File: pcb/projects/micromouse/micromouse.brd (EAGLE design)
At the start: 80 x 100 mm, 52 parts, among them M1 332-06, M2 332-06, U1 DSPIC33FJ64MC804-H/PTTQFP44_1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, U2 UA78M33CKCS, U3 UA78M05CKCS

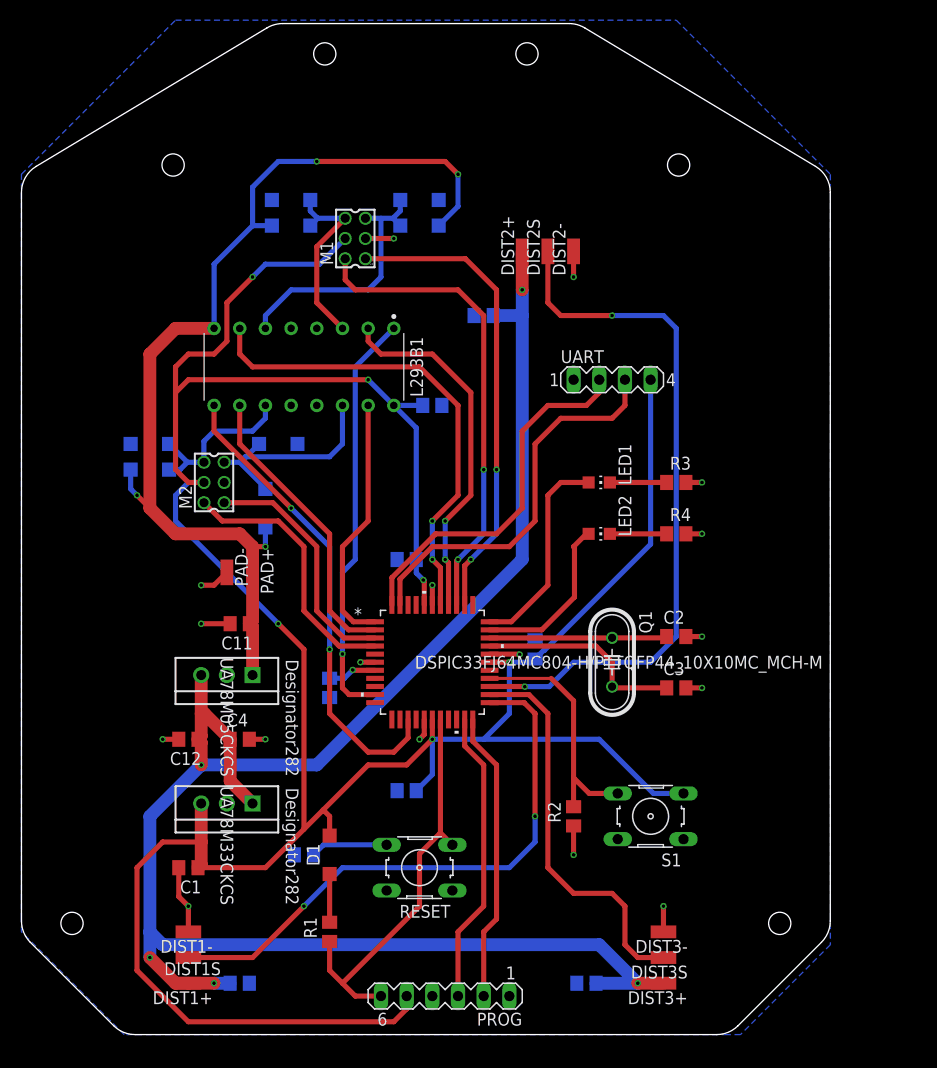
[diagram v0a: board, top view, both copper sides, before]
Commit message: Import new board shape
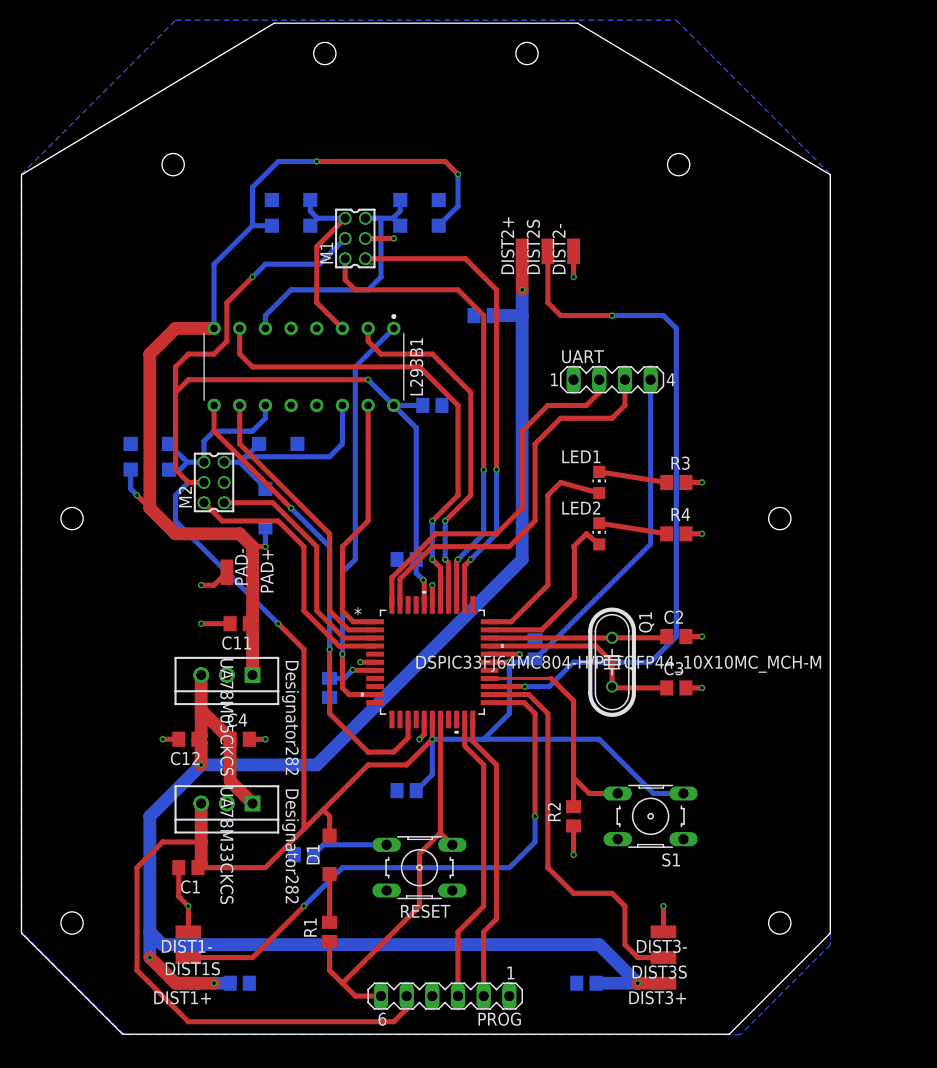
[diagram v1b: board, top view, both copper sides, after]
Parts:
- turned LED1 to 0 degrees
- turned LED2 to 0 degrees
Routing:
- net LED2: track 16.8 -> 18.2 mm
- net LED1: track 20.7 -> 21.9 mm
- net N$13: track 5.62 -> 6.75 mm
- net N$12: track 5.62 -> 6.75 mm
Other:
- outline, holes or cut-outs redrawn
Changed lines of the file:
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@@
 </layers>
 <board>
-<fusionsync huburn="a.YnVzaW5lc3M6bXl0dW03NTE" projecturn="a.YnVzaW5lc3M6bXl0dW03NTEjMjAyMjAxMTg0ODY2MTA4MzE" f3durn="urn:adsk.wipprod:dm.lineage:0fkBe2gqQnChnMdfLTDDww" pcbguid="" lastpulledtime="2022-01-21T13:45:10Z" lastsyncedchangeguid="" latestrevisionid="6a0397da-a106-4a81-945a-c83413a9f04e" lastsyncedrevisionid="6a0397da-a106-4a81-945a-c83413a9f04e" lastboardhashguid="eefc5839-d65c-dcc0-8c7d-7e0dee3f5582" lastpushedtime="2022-01-25T12:08:33Z" linktopcb3d="true"/>
+<fusionsync huburn="a.YnVzaW5lc3M6bXl0dW03NTE" projecturn="a.YnVzaW5lc3M6bXl0dW03NTEjMjAyMjAxMTg0ODY2MTA4MzE" f3durn="urn:adsk.wipprod:dm.lineage:keifWLGXSk6oYHrA5SEV4A" pcbguid="" lastpulledtime="2022-01-28T17:10:11Z" lastsyncedchangeguid="" latestrevisionid="07cd521d-d48a-4444-940e-28573b863771" lastsyncedrevisionid="07cd521d-d48a-4444-940e-28573b863771" lastboardhashguid="eefc5839-d65c-dcc0-8c7d-7e0dee3f5582" lastpushedtime="2022-01-25T12:08:33Z" linktopcb3d="true"/>
 <plain>
-<hole x="50" y="97" drill="2.2"/>
-<hole x="65" y="86.009" drill="2.2"/>
-<hole x="75" y="11" drill="2.2"/>
-<hole x="30" y="97" drill="2.2"/>
-<hole x="15" y="86.009" drill="2.2"/>
-<hole x="5" y="11" drill="2.2"/>
-<wire x1="80" y1="11.2426" x2="80" y2="83.3014" width="0" layer="20"/>
-<wire x1="80" y1="83.3014" x2="78.5435" y2="85.8739" width="0" layer="20" curve="59.0362"/>
-<wire x1="78.5435" y1="85.8739" x2="55.7125" y2="99.5725" width="0" layer="20"/>
-<wire x1="55.7125" y1="99.5725" x2="54.169" y2="100" width="0" layer="20" curve="30.9638"/>
-<wire x1="54.169" y1="100" x2="25.831" y2="100" width="0" layer="20"/>
-<wire x1="25.831" y1="100" x2="24.2875" y2="99.5725" width="0" layer="20" curve="30.9638"/>
-<wire x1="24.2875" y1="99.5725" x2="1.4565" y2="85.8739" width="0" layer="20"/>
-<wire x1="1.4565" y1="85.8739" x2="0" y2="83.3014" width="0" layer="20" curve="59.0362"/>
-<wire x1="0" y1="83.3014" x2="0" y2="11.2426" width="0" layer="20"/>
-<wire x1="0" y1="11.2426" x2="0.8787" y2="9.1213" width="0" layer="20" curve="45"/>
-<wire x1="0.8787" y1="9.1213" x2="9.1213" y2="0.8787" width="0" layer="20"/>
-<wire x1="9.1213" y1="0.8787" x2="11.2426" y2="0" width="0" layer="20" curve="45"/>
-<wire x1="11.2426" y1="0" x2="68.7574" y2="0" width="0" layer="20"/>
-<wire x1="68.7574" y1="0" x2="70.8787" y2="0.8787" width="0" layer="20" curve="45"/>
-<wire x1="70.8787" y1="0.8787" x2="79.1213" y2="9.1213" width="0" layer="20"/>
-<wire x1="79.1213" y1="9.1213" x2="80" y2="11.2426" width="0" layer="20" curve="45"/>
 <wire x1="10.16" y1="0" x2="10.16" y2="69.85" width="0.1524" layer="48" style="shortdash"/>
 <wire x1="10.16" y1="69.85" x2="27.94" y2="87.63" width="0.1524" layer="48" style="shortdash"/>
@@
 because parts will be mounted
 there.</text>
+<circle x="75.005" y="11.038" locked="yes" radius="1.1" width="0" layer="20"/>
+<circle x="5.005" y="51.038" locked="yes" radius="1.1" width="0" layer="20"/>
+<circle x="30.005" y="97.038" locked="yes" radius="1.1" width="0" layer="20"/>
+<circle x="15.005" y="86.047" locked="yes" radius="1.1" width="0" layer="20"/>
+<circle x="5.005" y="11.038" locked="yes" radius="1.1" width="0" layer="20"/>
+<circle x="75.005" y="51.038" locked="yes" radius="1.1" width="0" layer="20"/>
+<circle x="50.005" y="97.038" locked="yes" radius="1.1" width="0" layer="20"/>
+<circle x="65.005" y="86.047" locked="yes" radius="1.1" width="0" layer="20"/>
+<wire x1="70.005" y1="0.038" x2="80.005" y2="10.038" width="0" layer="20" locked="yes"/>
+<wire x1="80.005" y1="10.038" x2="80.005" y2="85.038" width="0" layer="20" locked="yes"/>
+<wire x1="55.005" y1="100.038" x2="80.005" y2="85.038" width="0" layer="20" locked="yes"/>
+<wire x1="55.005" y1="100.038" x2="25.005" y2="100.038" width="0" layer="20" locked="yes"/>
+<wire x1="25.005" y1="100.038" x2="0.005" y2="85.038" width="0" layer="20" locked="yes"/>
+<wire x1="0.005" y1="10.038" x2="0.005" y2="85.038" width="0" layer="20" locked="yes"/>
+<wire x1="10.005" y1="0.038" x2="0.005" y2="10.038" width="0" layer="20" locked="yes"/>
+<wire x1="70.005" y1="0.038" x2="10.005" y2="0.038" width="0" layer="20" locked="yes"/>
 </plain>
 <attributes>
@@
 <attribute name="VALUE" x="17.4293" y="66.04" size="1.27" layer="27" rot="R270" align="top-center"/>
 </element>
-<element name="LED1" library="led" library_urn="urn:adsk.eagle:library:259" package="CHIP-LED0805" package3d_urn="urn:adsk.eagle:package:15818/2" value="" x="57.15" y="54.61" smashed="yes" rot="R270">
-<attribute name="NAME" x="59.055" y="58.42" size="1.27" layer="25" rot="R270"/>
-<attribute name="POPULARITY" value="68" x="19.05" y="-16.51" size="1.778" layer="27" rot="R270" display="off"/>
-<attribute name="VALUE" x="53.975" y="58.42" size="1.27" layer="27" rot="R270"/>
-</element>
-<element name="LED2" library="led" library_urn="urn:adsk.eagle:library:259" package="CHIP-LED0805" package3d_urn="urn:adsk.eagle:package:15818/2" value="" x="57.15" y="49.53" smashed="yes" rot="R270">
-<attribute name="NAME" x="59.055" y="53.34" size="1.27" layer="25" rot="R270"/>
-<attribute name="POPULARITY" value="68" x="3.81" y="30.48" size="1.778" layer="27" rot="R270" display="off"/>
-<attribute name="VALUE" x="53.975" y="53.34" size="1.27" layer="27" rot="R270"/>
+<element name="LED1" library="led" library_urn="urn:adsk.eagle:library:259" package="CHIP-LED0805" package3d_urn="urn:adsk.eagle:package:15818/2" value="" x="57.15" y="54.61" smashed="yes">
+<attribute name="NAME" x="53.34" y="56.515" size="1.27" layer="25"/>
+<attribute name="POPULARITY" value="68" x="128.27" y="16.51" size="1.778" layer="27" display="off"/>
+<attribute name="VALUE" x="53.34" y="51.435" size="1.27" layer="27"/>
+</element>
+<element name="LED2" library="led" library_urn="urn:adsk.eagle:library:259" package="CHIP-LED0805" package3d_urn="urn:adsk.eagle:package:15818/2" value="" x="57.15" y="49.53" smashed="yes">
+<attribute name="NAME" x="53.34" y="51.435" size="1.27" layer="25"/>
+<attribute name="POPULARITY" value="68" x="76.2" y="-3.81" size="1.778" layer="27" display="off"/>
+<attribute name="VALUE" x="53.34" y="46.355" size="1.27" layer="27"/>
 </element>
 <element name="M1" library="con-garry" library_urn="urn:adsk.eagle:library:147" package="332-06" package3d_urn="urn:adsk.eagle:package:6811/1" value="332-06" x="33.02" y="78.74" smashed="yes" rot="R90">
@@
 <wire x1="48.45" y1="40.83" x2="52.07" y2="44.45" width="0.508" layer="1"/>
 <wire x1="52.07" y1="53.34" x2="52.07" y2="44.45" width="0.508" layer="1"/>
-<wire x1="56.1" y1="54.61" x2="53.34" y2="54.61" width="0.508" layer="1"/>
+<wire x1="57.15" y1="53.56" x2="53.34" y2="54.61" width="0.508" layer="1"/>
 <wire x1="53.34" y1="54.61" x2="52.07" y2="53.34" width="0.508" layer="1"/>
 </signal>
@@
 <wire x1="54.7" y1="48.17" x2="54.61" y2="48.26" width="0.508" layer="1"/>
 <wire x1="54.61" y1="48.26" x2="55.88" y2="49.53" width="0.508" layer="1"/>
-<wire x1="55.88" y1="49.53" x2="56.1" y2="49.53" width="0.508" layer="1"/>
+<wire x1="55.88" y1="49.53" x2="57.15" y2="48.48" width="0.508" layer="1"/>
 </signal>
 <signal name="N$12">
 <contactref element="LED1" pad="C"/>
 <contactref element="R3" pad="1"/>
-<wire x1="58.2" y1="54.61" x2="63.82" y2="54.61" width="0.508" layer="1"/>
+<wire x1="57.15" y1="55.66" x2="63.82" y2="54.61" width="0.508" layer="1"/>
 </signal>
 <signal name="N$13">
 <contactref element="LED2" pad="C"/>
 <contactref element="R4" pad="1"/>
-<wire x1="58.2" y1="49.53" x2="63.82" y2="49.53" width="0.508" layer="1"/>
+<wire x1="57.15" y1="50.58" x2="63.82" y2="49.53" width="0.508" layer="1"/>
 </signal>
 </signals>
@@
 packages will not be understood (or retained) with this version.
 </note>
+<note version="8.5" severity="warning">
+Since Version 8.5, EAGLE supports locking for holes, vias, wires and polygons.
+The locking property on all objects of these types will not be understood in this version.
+</note>
 </compatibility>

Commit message: Replace some pin connectors
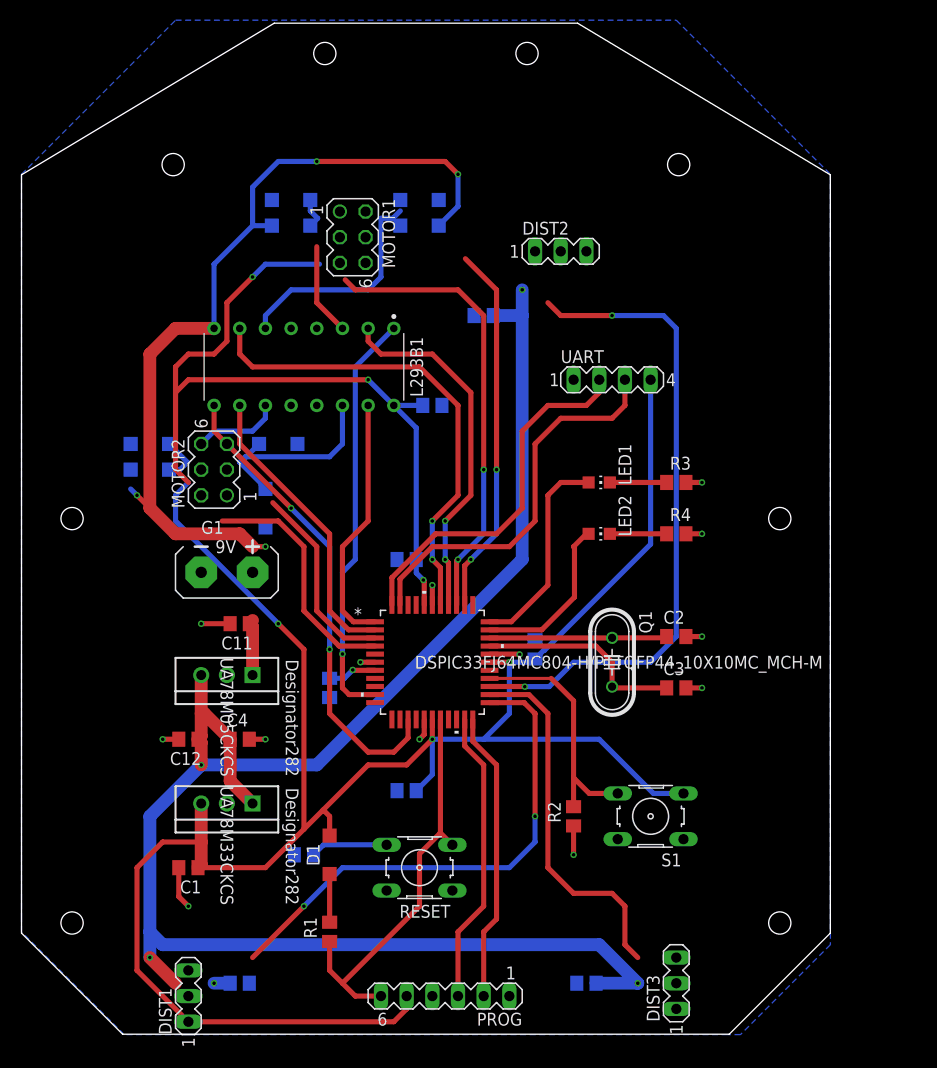
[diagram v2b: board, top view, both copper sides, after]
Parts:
- removed DIST1+, DIST1-, DIST1S, DIST2+, DIST2-, DIST2S, DIST3+, DIST3-, DIST3S, PAD+, PAD-: (no value), wirepad:SMD1,27-2,54
- removed M1, M2: 332-06, con-garry:332-06
- added DIST1, DIST2, DIST3: (no value), con-lstb:MA03-1
- added G1: AB9V, battery:AB9V
- added MOTOR1, MOTOR2: (no value), con-lstb:MA03-2
- turned LED1 to 270 degrees
- turned LED2 to 270 degrees
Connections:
- net +5V: now also DIST1.3, DIST2.3, DIST3.3; no longer DIST1+.1, DIST2+.1, DIST3+.1
- net DSENS1: now also DIST1.2; no longer DIST1S.1
- net DSENS2: now also DIST2.2; no longer DIST2S.1
- net DSENS3: now also DIST3.2; no longer DIST3S.1
- net GND: now also DIST1.1, DIST2.1, DIST3.1, G1.-, MOTOR1.3, MOTOR2.3; no longer DIST1-.1, DIST2-.1, DIST3-.1, M1.3, M2.3, PAD-.1
- net M1+: now also D2.C, D4.A, MOTOR1.2; no longer D3.C, D5.A, M1.6
- net M1-: now also D3.C, D5.A, MOTOR1.1; no longer D2.C, D4.A, M1.5
- net M1_EA: now also MOTOR1.6; no longer M1.2
- net M1_EB: now also MOTOR1.5; no longer M1.1
- net M2+: now also MOTOR2.2; no longer M2.6
- net M2-: now also MOTOR2.1; no longer M2.5
- net M2_EA: now also MOTOR2.6; no longer M2.2
- net M2_EB: now also MOTOR2.5; no longer M2.1
- net PAD+: now also G1.+; no longer PAD+.1
- net VDD: now also MOTOR1.4, MOTOR2.4; no longer M1.4, M2.4
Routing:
- net GND: track 41.5 -> 28.0 mm, vias 17 -> 13
- net PAD+: track 100.3 -> 89.2 mm
- net +5V: track 181.0 -> 170.9 mm
- net M1_EB: track 46.7 -> 36.8 mm
- net M1+: track 19.0 -> 9.13 mm
- net VDD: track 292.7 -> 286.0 mm
- net DSENS1: track 56.7 -> 50.3 mm
- net DSENS2: track 69.8 -> 64.8 mm
- net M2_EB: track 24.2 -> 19.4 mm
- net M2+: track 16.7 -> 13.0 mm
- net M2_EA: track 26.5 -> 24.0 mm
- net DSENS3: track 39.1 -> 36.6 mm
- net M1_EA: track 47.0 -> 44.9 mm
- net M2-: track 22.6 -> 21.1 mm
- net LED2: track 18.2 -> 16.8 mm
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
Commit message: Routing for new PCB
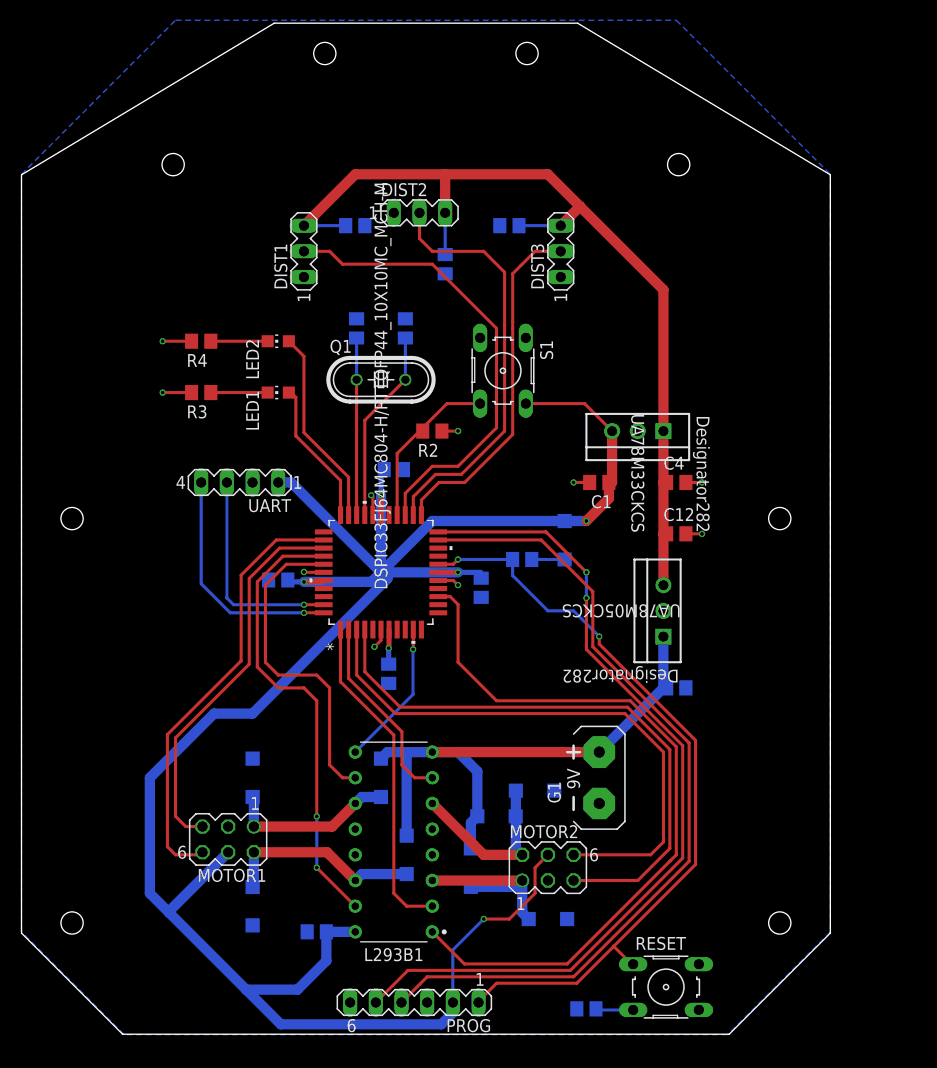
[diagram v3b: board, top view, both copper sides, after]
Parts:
- C8: value (none) -> 100nF
- R1: value 47k -> 10k
- moved C7 75.8 mm to (33.0, 80.0)
- moved C10 75.3 mm to (48.3, 80.0)
- moved DIST1 74.5 mm to (27.9, 77.5)
- moved DIST3 73.3 mm to (53.3, 77.5)
- moved D2 71.8 mm to (22.9, 12.7), turned to 270 degrees
- moved D4 62.2 mm to (38.1, 17.8), turned to 270 degrees
- moved MOTOR1 60.8 mm to (20.4, 19.3), turned to 180 degrees
- moved D3 57.3 mm to (22.9, 25.4), turned to 90 degrees
- moved C1 55.7 mm to (57.1, 54.6)
- moved D5 55.3 mm to (35.6, 25.4), turned to 270 degrees
- moved U2 54.8 mm to (61.0, 59.7)
- moved D6 54.0 mm to (52.1, 11.4)
- moved C6 53.3 mm to (29.2, 10.2), turned to 0 degrees
- moved C12 52.4 mm to (64.8, 49.5), turned to 0 degrees
- moved MOTOR2 51.4 mm to (52.1, 16.5), turned to 0 degrees
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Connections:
- net N$1 renamed VCAP
- net PAD+ renamed +9V
- removed net N$6: PROG.6, R1.1, RESET.3, U1.18
- removed net N$8: PROG.3, U1.21
- removed net N$9: PROG.2, U1.22
- new net ICSP_CLOCK: PROG.5, U1.22
- new net ICSP_DATA: PROG.4, U1.21
- new net MCLR: PROG.1, R1.1, RESET.1, U1.18
- net DSENS1: now also U1.25; no longer U1.23
- net DSENS2: now also U1.24; no longer U1.25
- net DSENS3: now also U1.23; no longer U1.24
- net GND: now also PROG.3, UART.2; no longer PROG.4, UART.1
- net M1+: now also L293B1.OUTPUT4; no longer L293B1.OUTPUT1
- net M1-: now also L293B1.OUTPUT3; no longer L293B1.OUTPUT2
- net M1_D1: now also L293B1.INPUT3, U1.38; no longer L293B1.INPUT1, U1.37
- net M1_D2: now also L293B1.INPUT4, U1.37; no longer L293B1.INPUT2, U1.38
- net M1_EA: now also U1.35; no longer U1.36
- net M1_EB: now also U1.36; no longer U1.35
- net M1_PWM: now also L293B1.ENABLE2; no longer L293B1.ENABLE1
- net M2+: now also L293B1.OUTPUT2; no longer L293B1.OUTPUT3
- net M2-: now also L293B1.OUTPUT1; no longer L293B1.OUTPUT4
- net M2_D1: now also L293B1.INPUT1, U1.1; no longer L293B1.INPUT3, U1.2
- net M2_D2: now also L293B1.INPUT2, U1.2; no longer L293B1.INPUT4, U1.1
- net M2_EA: now also U1.3; no longer U1.4
- net M2_EB: now also U1.4; no longer U1.3
- net M2_PWM: now also L293B1.ENABLE1; no longer L293B1.ENABLE2
- net N$3: now also RESET.3; no longer RESET.4
- net RX: now also UART.4; no longer UART.2
- net VDD: now also PROG.2, S1.2, UART.1; no longer PROG.5, S1.3, UART.4
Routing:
- net ICSP_CLOCK: track 0.00 -> 84.8 mm, vias 0 -> 2
- net ICSP_DATA: track 0.00 -> 82.3 mm
- net +5V: track 170.9 -> 91.1 mm, vias 5 -> 0
- net MCLR: track 0.00 -> 76.5 mm, vias 0 -> 2
- net VDD: track 286.0 -> 217.0 mm, vias 6 -> 5
- net N$6: track 40.8 -> 0.00 mm
- net M2_EB: track 19.4 -> 58.2 mm
- net M2_EA: track 24.0 -> 56.3 mm
- net +9V: track 89.2 -> 57.6 mm, vias 4 -> 0
- net N$8: track 29.2 -> 0.00 mm
- net N$9: track 28.9 -> 0.00 mm
- net M2_PWM: track 47.0 -> 73.6 mm, vias 2 -> 0
- net M1_PWM: track 41.2 -> 14.5 mm
- net DSENS2: track 64.8 -> 41.6 mm, vias 2 -> 0
- net TX: track 38.9 -> 21.3 mm, vias 0 -> 1
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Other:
- board text added: "Motor 1"
- board text added: "Motor 2"
- board text added: "Sensor 1"
- board text added: "Sensor 2"
- board text added: "Sensor 3"
- board text removed: "Motor"
- board text removed: "Sensor"
